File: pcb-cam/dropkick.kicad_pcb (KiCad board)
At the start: 2 copper layers, 44.5 x 50.8 mm, 52 parts, among them J1 Conn_01x10, SW1 450405020524, SW2 KMR211NG_LFS, U1 SPX3819-3.3, U2 MCP73831T-2ACI/OT, U3 CAM-M8C-0, U4 ATSAMD21G18A-AUT, U5 DPS310XTSA1, U6 MPU-6050, X1 USB micro-B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

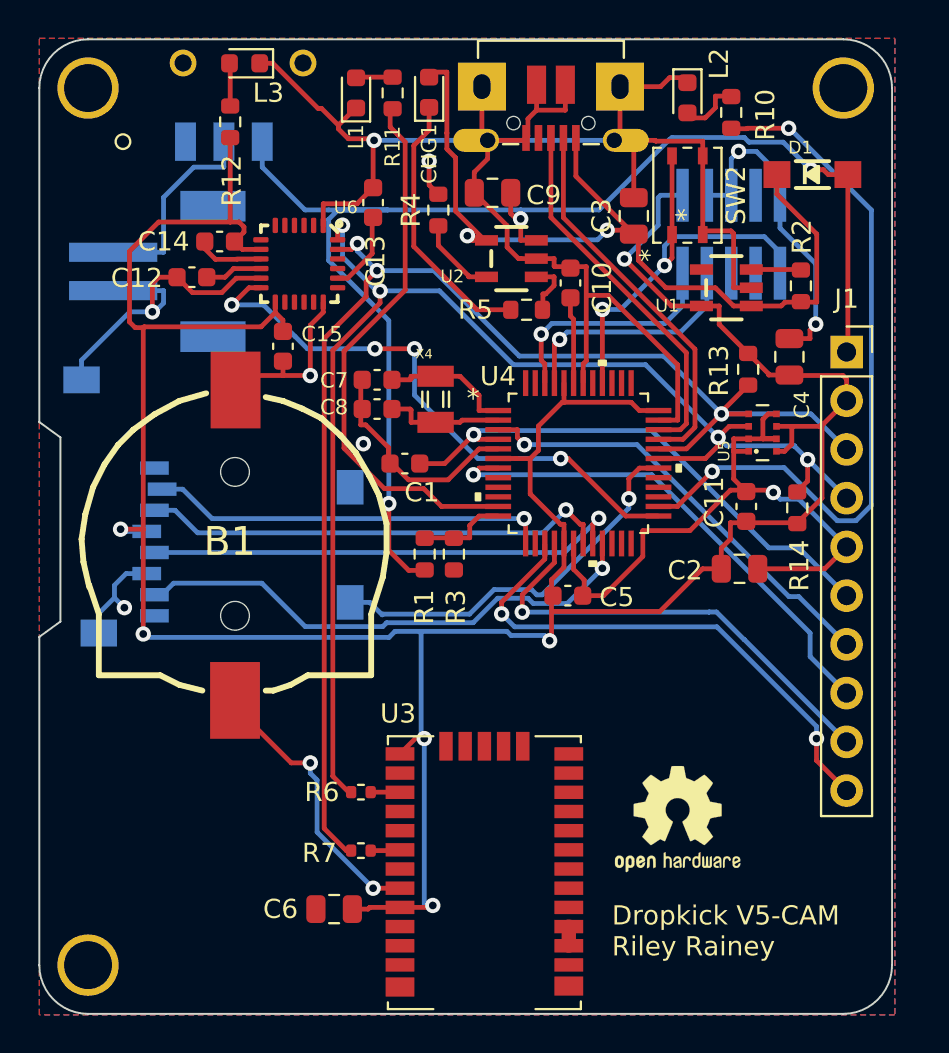
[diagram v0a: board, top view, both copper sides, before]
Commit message: Switch to 2.0mm pads and added SWDIO/SWCLK pads to flash w/o header
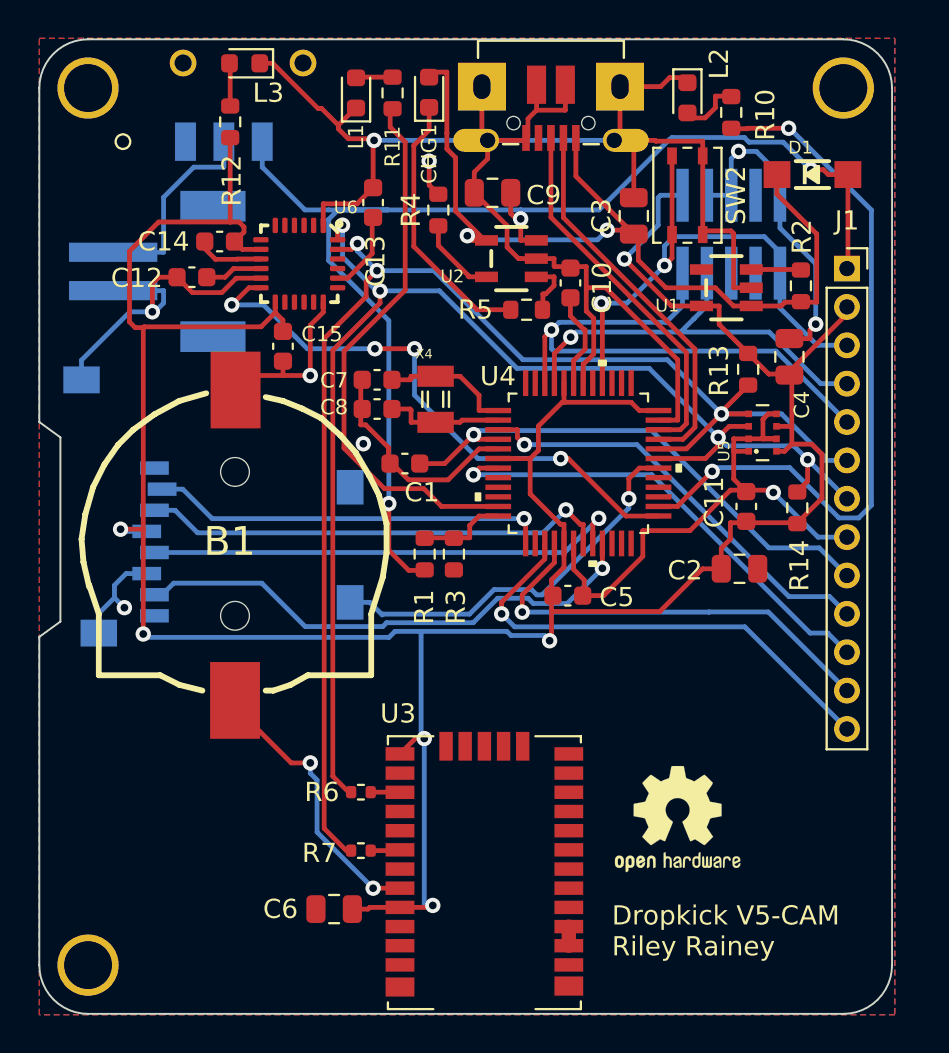
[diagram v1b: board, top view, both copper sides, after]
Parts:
- J1: value Conn_01x10 -> Conn_01x13; footprint Connector_PinSocket_2.54mm:PinSocket_1x10_P2.54mm_Vertical -> Connector_PinSocket_2.00mm:PinSocket_1x13_P2.00mm_Vertical
- moved J1 4.35 mm to (105.6, 56.4)
- renumbered JP1 to J2
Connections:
- net /D11 renamed /INT
- J1 pad 10: /D1 -> /A0
- J1 pad 3: /SCL -> /~{RESET}
- J1 pad 4: /SDA -> /SWCLK
- J1 pad 5: GND -> /SWDIO
- J1 pad 6: /AREF -> /SCL
- J1 pad 7: /A0 -> /SDA
- J1 pad 8: /A1 -> GND
- J1 pad 9: /D0 -> /AREF
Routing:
- net /SWDIO: track 12.3 -> 29.9 mm
- net /SWCLK: track 12.5 -> 23.3 mm
- net /~{RESET}: track 22.6 -> 28.9 mm
- net GND: track 190.2 -> 185.6 mm
- net VBAT: track 72.7 -> 68.3 mm
- net /D1: track 27.4 -> 25.1 mm, vias 2 -> 1
- net /A1: track 26.4 -> 24.8 mm
- net /D0: track 24.0 -> 22.9 mm
- net /A0: track 23.0 -> 22.4 mm
- net Net-(U4-VDDCORE): track 4.44 -> 4.96 mm
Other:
- board text added: "/RESET"
- board text added: "3.3V"
- board text added: "SWCLK"
- board text added: "SWDIO"
- board text removed: "+3.3V"

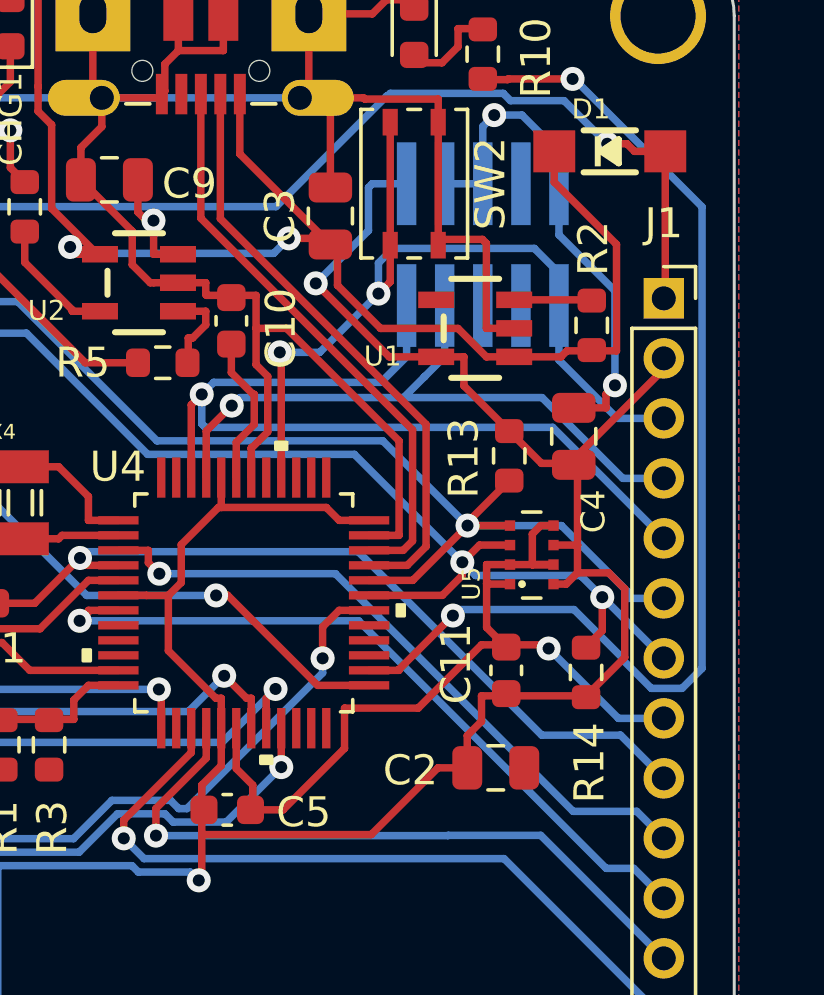
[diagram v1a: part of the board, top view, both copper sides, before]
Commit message: Added extra CAP per DPS310 datasheet
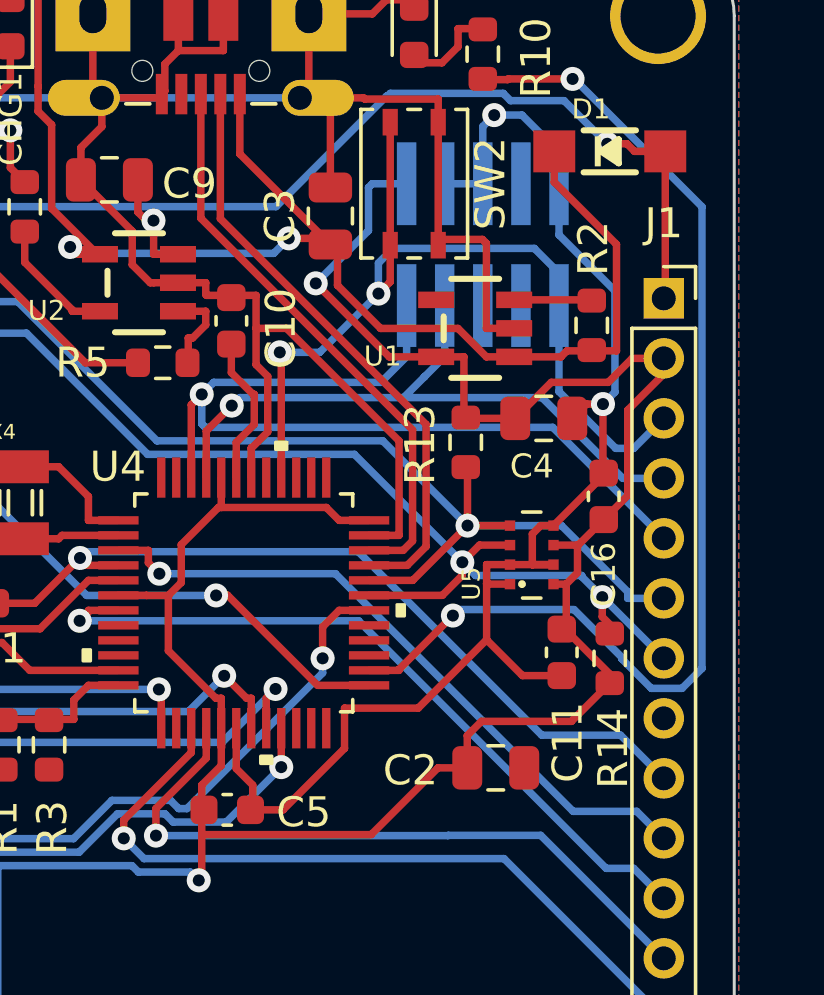
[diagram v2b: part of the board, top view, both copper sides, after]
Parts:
- added C16: 0.1µF, Capacitor_SMD:C_0603_1608Metric, F.Cu at (103.6, 63.0)
- CHG1: value ORANGE LED -> ORANGE
- L1, L3: value GREEN LED -> GREEN
- L2: value RED LED -> RED
- moved C11 1.94 mm to (102.2, 68.2), turned to -90 degrees
- moved R13 1.52 mm to (99.0, 61.2)
- moved C4 1.17 mm to (101.6, 60.4), turned to 0 degrees
- moved R14 0.92 mm to (103.8, 68.4)
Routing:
- net +3V3: track 158.7 -> 161.2 mm
- net /~{RESET}: track 28.9 -> 30.4 mm
- net GND: track 185.6 -> 185.8 mm, vias 9 -> 8

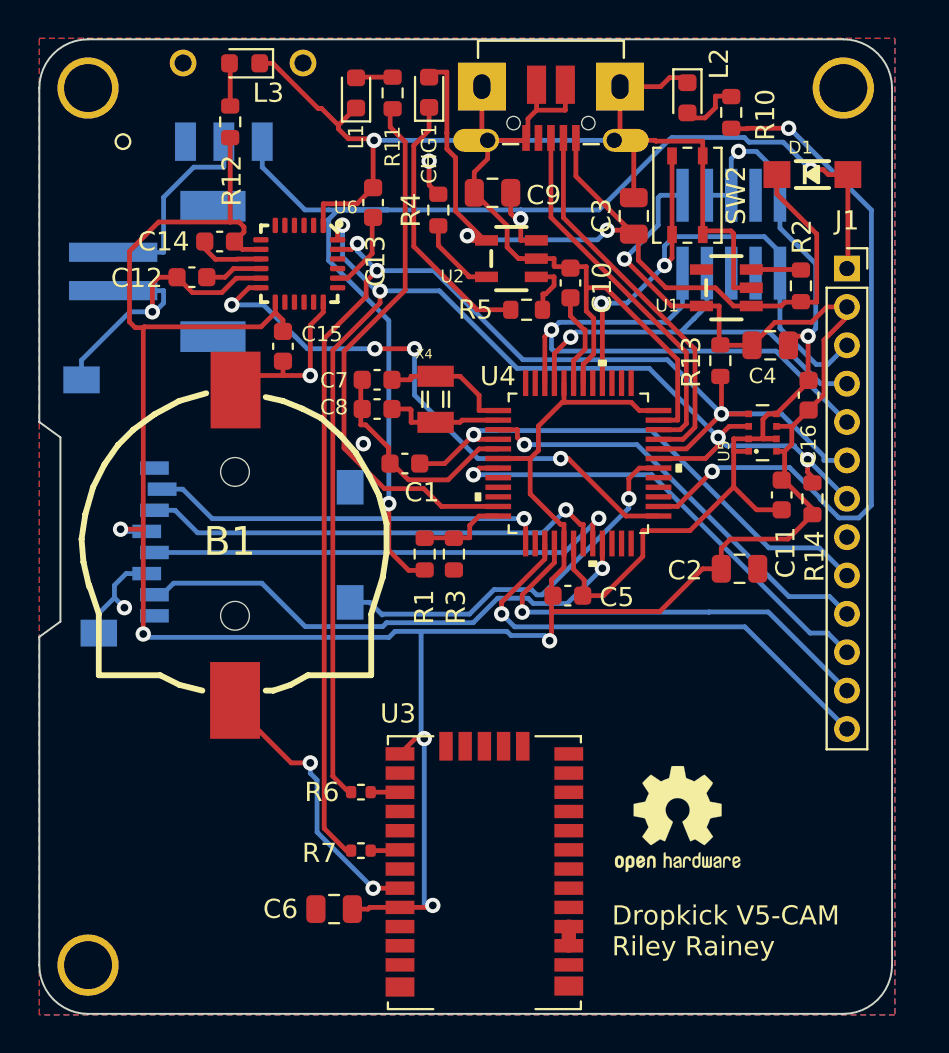
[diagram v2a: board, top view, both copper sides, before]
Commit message: Add boxes to schematic; clean up PCB placement; use PCBWay gerber settings
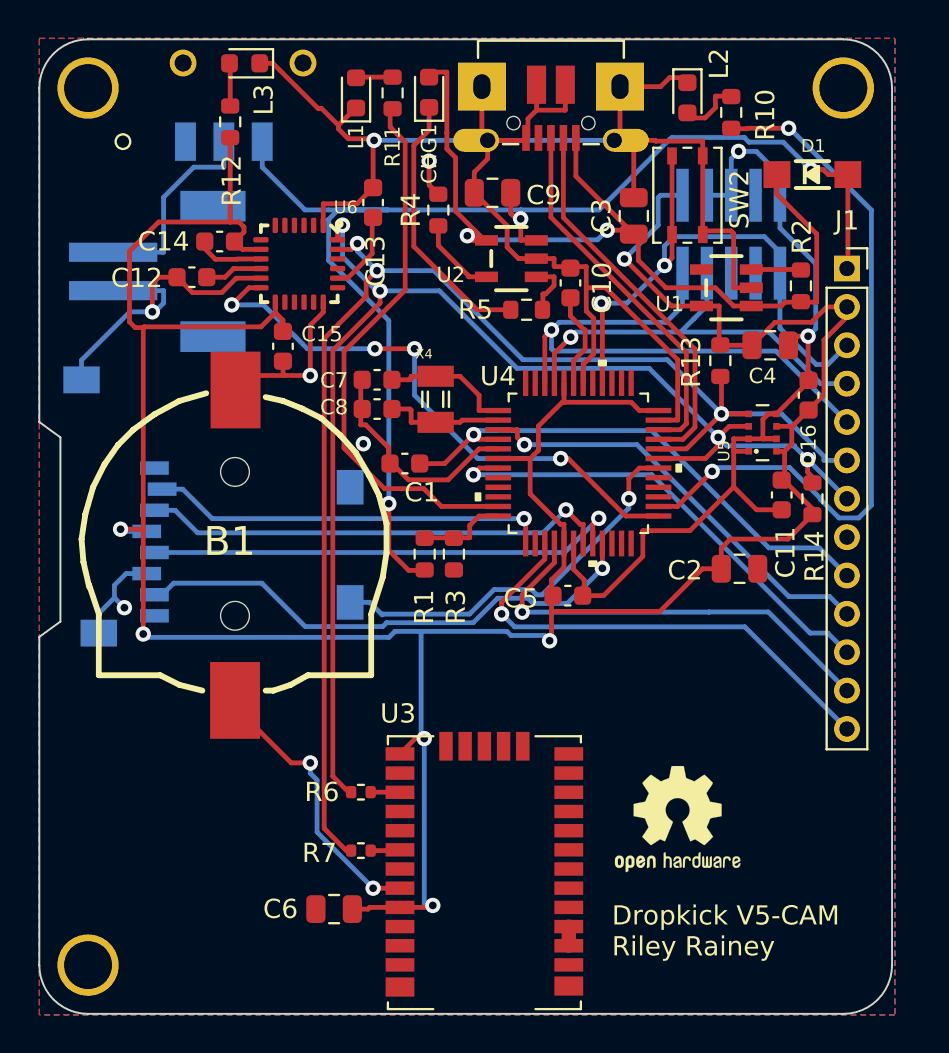
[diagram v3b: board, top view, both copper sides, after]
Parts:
- U4: value ATSAMD21G18A-AUT -> ATSAMD21G18A-AU
- moved REF2 1.81 mm to (91.8, 69.4)
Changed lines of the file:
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@@
       (disableapertmacros false)
       (usegerberextensions false)
-      (usegerberattributes true)
-      (usegerberadvancedattributes true)
+      (usegerberattributes false)
+      (usegerberadvancedattributes false)
       (creategerberjobfile true)
       (dashed_line_dash_ratio 12.000000)
@@
     (property "Sheetname" "")
     (attr smd)
-    (fp_text reference "SW2" (at 0 2.54 90) (layer "F.SilkS")
+    (fp_text reference "SW2" (at -0.222 2.718 90) (layer "F.SilkS")
         (effects (font (size 1 1) (thickness 0.15)))
     )
@@
     (property "Sheetname" "")
     (attr smd)
-    (fp_text reference "C5" (at 2.549 0.083) (layer "F.SilkS")
+    (fp_text reference "C5" (at -2.45 0.15) (layer "F.SilkS")
         (effects (font (size 1 1) (thickness 0.15)))
     )
@@
     (property "Sheetname" "")
     (fp_text reference "U1" (at -1.32 -3.7079 180) (layer "F.SilkS")
-        (effects (font (size 0.666496 0.666496) (thickness 0.146304)) (justify left bottom))
+        (effects (font (size 0.8 0.8) (thickness 0.146304)) (justify left bottom))
     )
     (fp_text value "SPX3819-3.3" (at 1.978 0.635 90) (layer "F.Fab")
@@
     (property "ki_keywords" "LED diode")
     (attr smd)
-    (fp_text reference "L3" (at -1.238 -1.544) (layer "F.SilkS")
+    (fp_text reference "L3" (at -1 -1.9 90) (layer "F.SilkS")
         (effects (font (size 1 1) (thickness 0.15)))
     )
@@
     (property "Sheetfile" "dropkick.kicad_sch")
     (property "Sheetname" "")
-    (fp_text reference "D1" (at -1.27 -1.016) (layer "F.SilkS")
+    (fp_text reference "D1" (at -0.6 -1.1) (layer "F.SilkS")
         (effects (font (size 0.666496 0.666496) (thickness 0.146304)) (justify left bottom))
     )
@@
   (footprint "lib_fp:ATSAMD21G15B-AU" (layer "F.Cu")
     (at 91.6 66.55)
-    (property "Manufacturer Part" "ATSAMD21G18A-AUT")
+    (property "Manufacturer Part" "ATSAMD21G18A-AU")
     (property "Sheetfile" "dropkick.kicad_sch")
     (property "Sheetname" "")
@@
         (effects (font (size 1 1) (thickness 0.15)))
     )
-    (fp_text value "ATSAMD21G18A-AUT" (at 0 0) (layer "F.SilkS") hide
+    (fp_text value "ATSAMD21G18A-AU" (at 0 0) (layer "F.SilkS") hide
         (effects (font (size 1 1) (thickness 0.15)))
     )
@@
     (property "Sheetfile" "dropkick.kicad_sch")
     (property "Sheetname" "")
-    (fp_text reference "U2" (at -1.32 -3.7079 180) (layer "F.SilkS")
-        (effects (font (size 0.666496 0.666496) (thickness 0.146304)) (justify left bottom))
+    (fp_text reference "U2" (at -1.32 -3.9079 180) (layer "F.SilkS")
+        (effects (font (size 0.8 0.8) (thickness 0.146304)) (justify left bottom))
     )
     (fp_text value "MCP73831T-2ACI/OT" (at 1.978 0.635 90) (layer "F.Fab")
@@
     (property "Sheetfile" "dropkick.kicad_sch")
     (property "Sheetname" "")
-    (fp_text reference "X3" (at 1.18 -7.69 270) (layer "B.SilkS")
-        (effects (font (size 0.666496 0.666496) (thickness 0.146304)) (justify right bottom mirror))
+    (fp_text reference "X3" (at -2.2 -12.94 270) (layer "B.SilkS")
+        (effects (font (size 0.8 0.8) (thickness 0.146304)) (justify right bottom mirror))
     )
     (fp_text value "microsd" (at 1.18 -8.833 270) (layer "B.Fab")
@@
     (property "Sheetname" "")
     (attr smd)
-    (fp_text reference "J2" (at -8.509 -1.905) (layer "B.SilkS")
+    (fp_text reference "J2" (at -7.768 -0.01) (layer "B.SilkS")
         (effects (font (size 1 1) (thickness 0.15)) (justify mirror))
     )
@@
   )
   (footprint "lib_fp:OSHW-Logo2_14.6x12mm_SilkScreen" locked (layer "B.Cu")
-    (at 90.932 70.993 180)
+    (at 91.8 69.4 180)
     (descr "Open Source Hardware Symbol")
     (tags "Logo Symbol OSHW")
@@
     (effects (font (size 0.8 0.8) (thickness 0.15)) (justify mirror))
   )
-  (gr_text "Dropkick V5-CAM\n\nCopyright (c) 2023 Riley Rainey\nhttps://GitHub.com/rrainey/dropkick/" (at 99.949 83.947) (layer "B.SilkS")
+  (gr_text "Dropkick V5-CAM\n\nCopyright (c) 2023 Riley Rainey\nhttps://GitHub.com/rrainey/dropkick/" (at 100.6 83.947) (layer "B.SilkS")
     (effects (font (size 1.2 1.2) (thickness 0.25)) (justify left mirror))
   )
